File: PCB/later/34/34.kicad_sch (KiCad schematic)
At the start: 57 parts, among them J1 USB_C_Receptacle_USB2.0, J2 Conn_01x04, J3 AVR-ISP-6, J4 Conn_01x04, SW1 SW_Push, SW10 SW_Push, SW11 SW_Push, SW12 SW_Push, SW13 SW_Push, SW14 SW_Push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

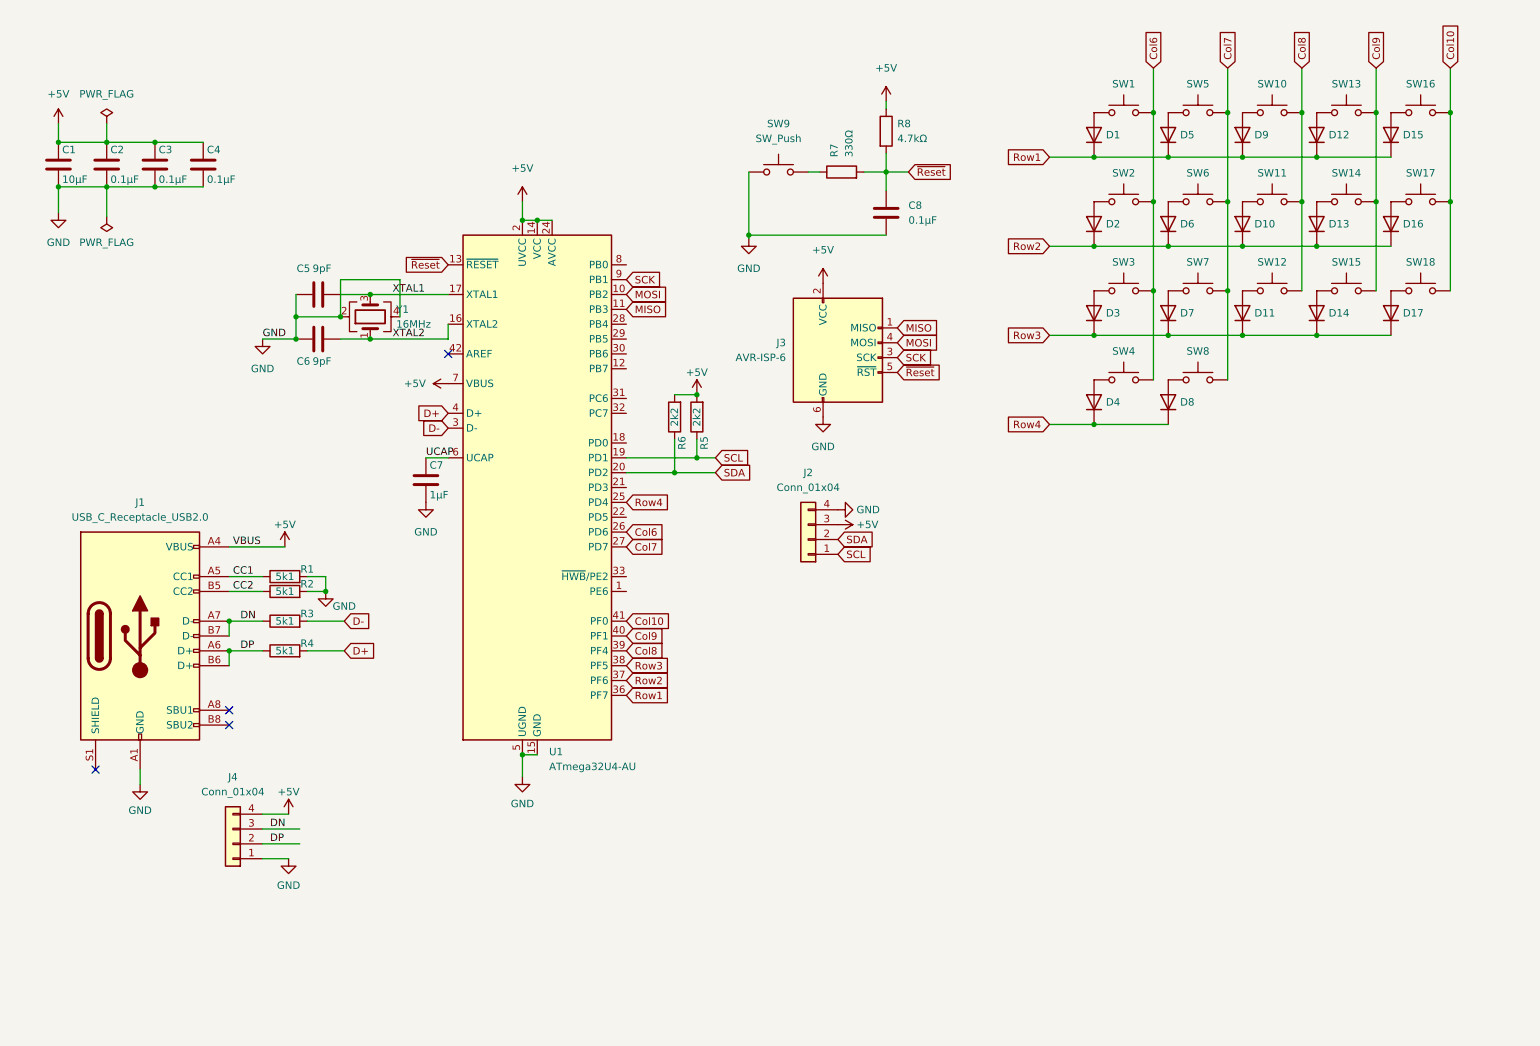
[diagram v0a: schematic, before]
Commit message: postpone i2c design
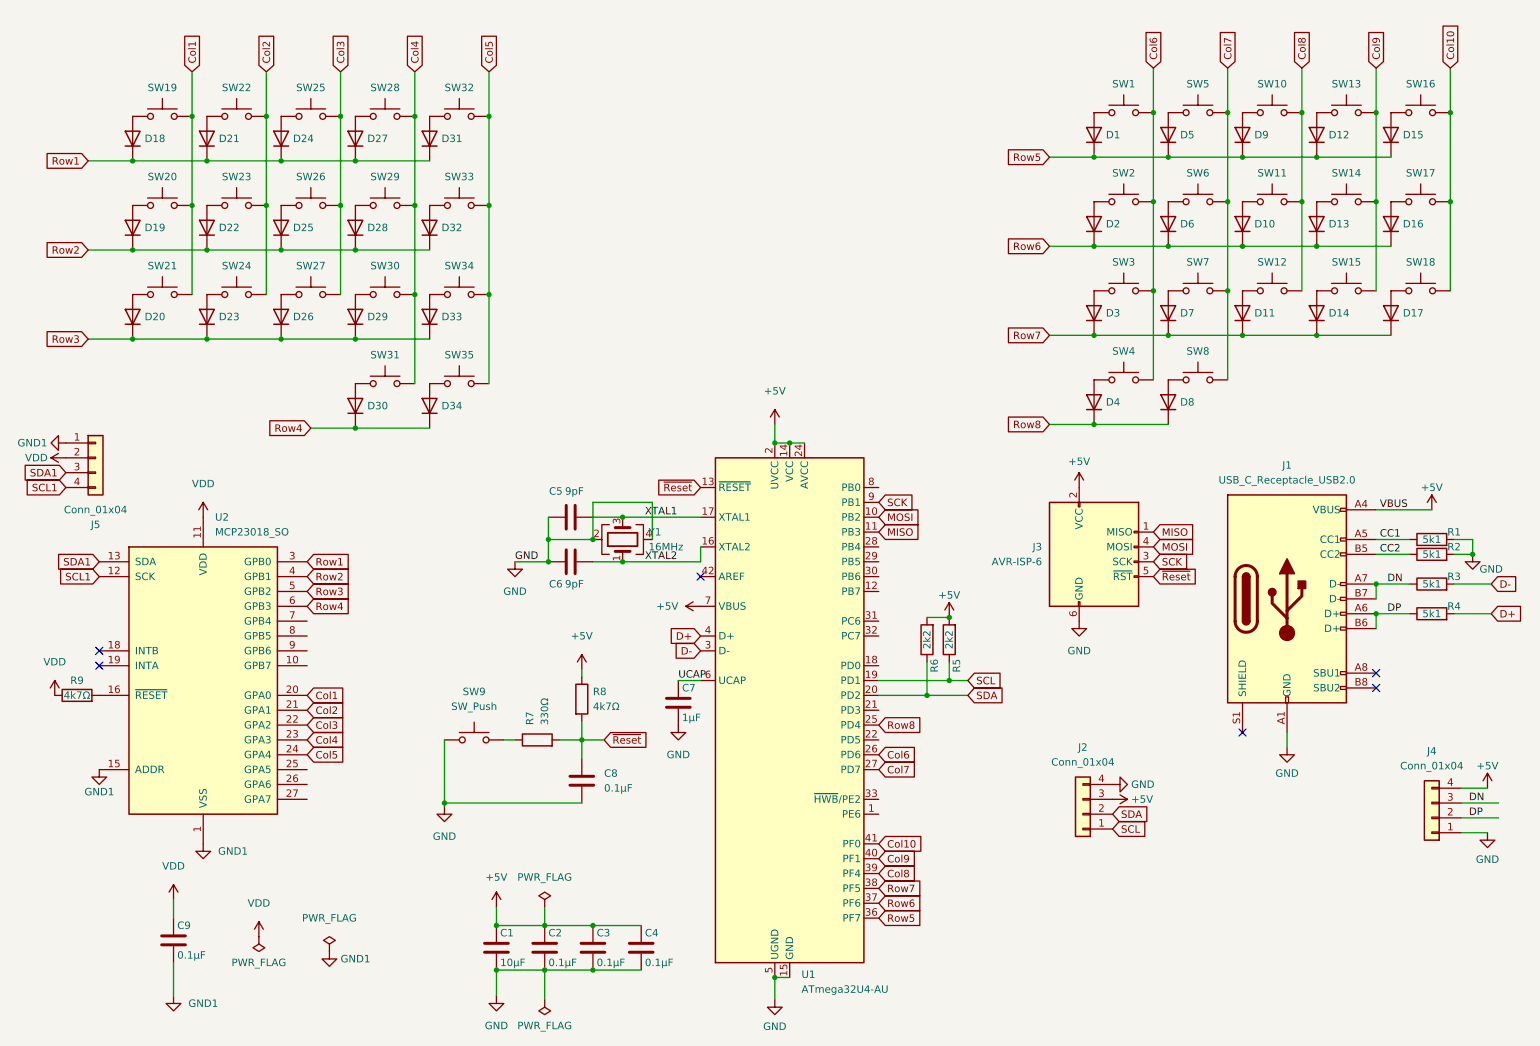
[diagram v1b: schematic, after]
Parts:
- added C9: 0.1µF, Capacitor_SMD:C_0402_1005Metric_Pad0.74x0.62mm_HandSolder, symbol Device:C
- added D18, D19, D20, D21, D22, D23, D24, D25, D26, D27, D28, D29, D30, D31, D32, D33, D34: 1N4148, Keyboard_Foostan:D3_SMD_v2, symbol Device:D
- added J5: Conn_01x04, Connector_JST:JST_PH_S4B-PH-K_1x04_P2.00mm_Horizontal, symbol Connector_Generic:Conn_01x04
- added R9: 4k7Ω, Resistor_SMD:R_0402_1005Metric_Pad0.72x0.64mm_HandSolder, symbol Device:R
- added SW19, SW20, SW21, SW22, SW23, SW24, SW25, SW26, SW27, SW28, SW29, SW30, SW31, SW32, SW33, SW34, SW35: SW_Push, Keyboard_JSA:MX_Hotswap_Choc_Solder, symbol Switch:SW_Push
- added U2: MCP23018_SO, Package_SO:SOIC-28W_7.5x17.9mm_P1.27mm, symbol Keyboard:MCP23018_SO
- R8: value 4.7kΩ -> 4k7Ω
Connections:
- net Row1: now also D18.1 (K), D21.1 (K), D24.1 (K), D27.1 (K), D31.1 (K), U2.3 (GPB0); no longer D1.1 (K), D12.1 (K), D15.1 (K), D5.1 (K), D9.1 (K), U1.36 (PF7)
- net Row2: now also D19.1 (K), D22.1 (K), D25.1 (K), D28.1 (K), D32.1 (K), U2.4 (GPB1); no longer D10.1 (K), D13.1 (K), D16.1 (K), D2.1 (K), D6.1 (K), U1.37 (PF6)
- net Row3: now also D20.1 (K), D23.1 (K), D26.1 (K), D29.1 (K), D33.1 (K), U2.5 (GPB2); no longer D11.1 (K), D14.1 (K), D17.1 (K), D3.1 (K), D7.1 (K), U1.38 (PF5)
- net Row4: now also D30.1 (K), D34.1 (K), U2.6 (GPB3); no longer D4.1 (K), D8.1 (K), U1.25 (PD4)
- new net: D18.2 (A), SW19.1
- new net: D27.2 (A), SW28.1
- new net: D34.2 (A), SW35.1
- new net: D33.2 (A), SW34.1
- new net: D32.2 (A), SW33.1
- new net: D29.2 (A), SW30.1
- new net: D25.2 (A), SW26.1
- new net: D23.2 (A), SW24.1
- new net: D30.2 (A), SW31.1
- new net: D31.2 (A), SW32.1
- new net: D19.2 (A), SW20.1
- new net: D21.2 (A), SW22.1
- new net: R9.2, U2.16 (~{RESET})
- new net: D20.2 (A), SW21.1
- new net: D24.2 (A), SW25.1
- new net: D22.2 (A), SW23.1
- new net: D28.2 (A), SW29.1
- new net: D26.2 (A), SW27.1
- new net Col1: SW19.2, SW20.2, SW21.2, U2.20 (GPA0)
- new net Col2: SW22.2, SW23.2, SW24.2, U2.21 (GPA1)
- new net Col3: SW25.2, SW26.2, SW27.2, U2.22 (GPA2)
- new net Col4: SW28.2, SW29.2, SW30.2, SW31.2, U2.23 (GPA3)
- new net Col5: SW32.2, SW33.2, SW34.2, SW35.2, U2.24 (GPA4)
- new net GND1: C9.2, J5.1 (Pin_1), U2.1 (VSS), U2.15 (ADDR)
- new net Row5: D1.1 (K), D12.1 (K), D15.1 (K), D5.1 (K), D9.1 (K), U1.36 (PF7)
- new net Row6: D10.1 (K), D13.1 (K), D16.1 (K), D2.1 (K), D6.1 (K), U1.37 (PF6)
- new net Row7: D11.1 (K), D14.1 (K), D17.1 (K), D3.1 (K), D7.1 (K), U1.38 (PF5)
- new net Row8: D4.1 (K), D8.1 (K), U1.25 (PD4)
- new net SCL1: J5.4 (Pin_4), U2.12 (SCK)
- new net SDA1: J5.3 (Pin_3), U2.13 (SDA)
- new net VDD: C9.1, J5.2 (Pin_2), R9.1, U2.11 (VDD)
- no-connect marks 4 -> 6
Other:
- moved on the sheet: C1, C2, C3, C4, C5, C6, C7, C8, J1, J2, J3, J4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
